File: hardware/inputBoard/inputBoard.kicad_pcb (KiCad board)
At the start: 2 copper layers, 198 x 34 mm, 17 parts, among them J2 LeftKeyConnector, J3 RightKeyConnector, J4 EncoderConnector, SW1 SW_Push, SW2 SW_Push, SW3 SW_Push, SW4 SW_Push, SW5 SW_Push, SW6 SW_Push, SW7 SW_Push, SW8 SW_Push, SW9 RotaryEncoder_Switch_MP

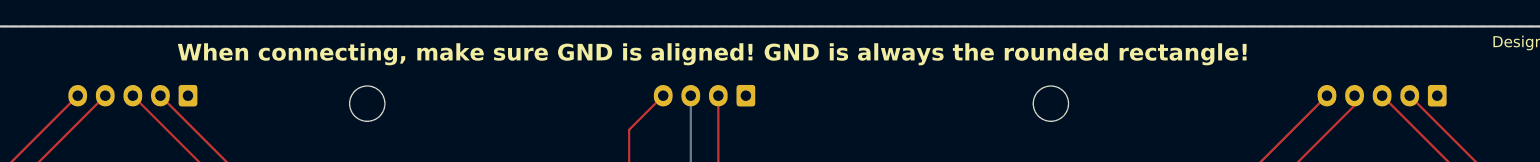
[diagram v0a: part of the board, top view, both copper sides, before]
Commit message: Label the connectors in the silkscreen
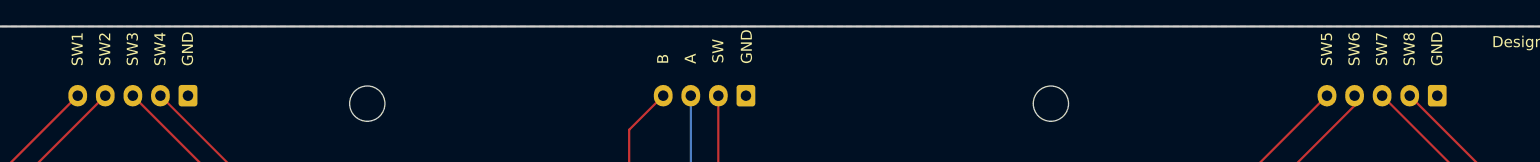
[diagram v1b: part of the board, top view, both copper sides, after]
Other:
- board text added: "A"
- board text added: "B"
- board text added: "GND"
- board text added: "SW"
- board text added: "SW1"
- board text added: "SW2"
- board text added: "SW3"
- board text added: "SW4"
- board text added: "SW5"
- board text added: "SW6"
- board text added: "SW7"
- board text added: "SW8"
- board text removed: "When connecting, make sure GND is aligned! GND is always the rounded rectangle!"
- board text removed: "When connecting, make sure GND is aligned! GND is always the rounded rectangle!r"

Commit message: update PCB routing and add debug probe
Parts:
- renumbered J2 to J101, J3 to J102, J4 to J103, SW1 to SW101, SW2 to SW102, SW3 to SW103, SW4 to SW104, SW5 to SW105, SW6 to SW106, SW7 to SW107, SW8 to SW108, SW9 to SW109
